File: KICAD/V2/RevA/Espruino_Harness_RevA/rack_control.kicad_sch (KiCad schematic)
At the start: 12 parts, among them Q1201 2N7002, Q1202 2N7002, U1201 MCP23017-E/SO

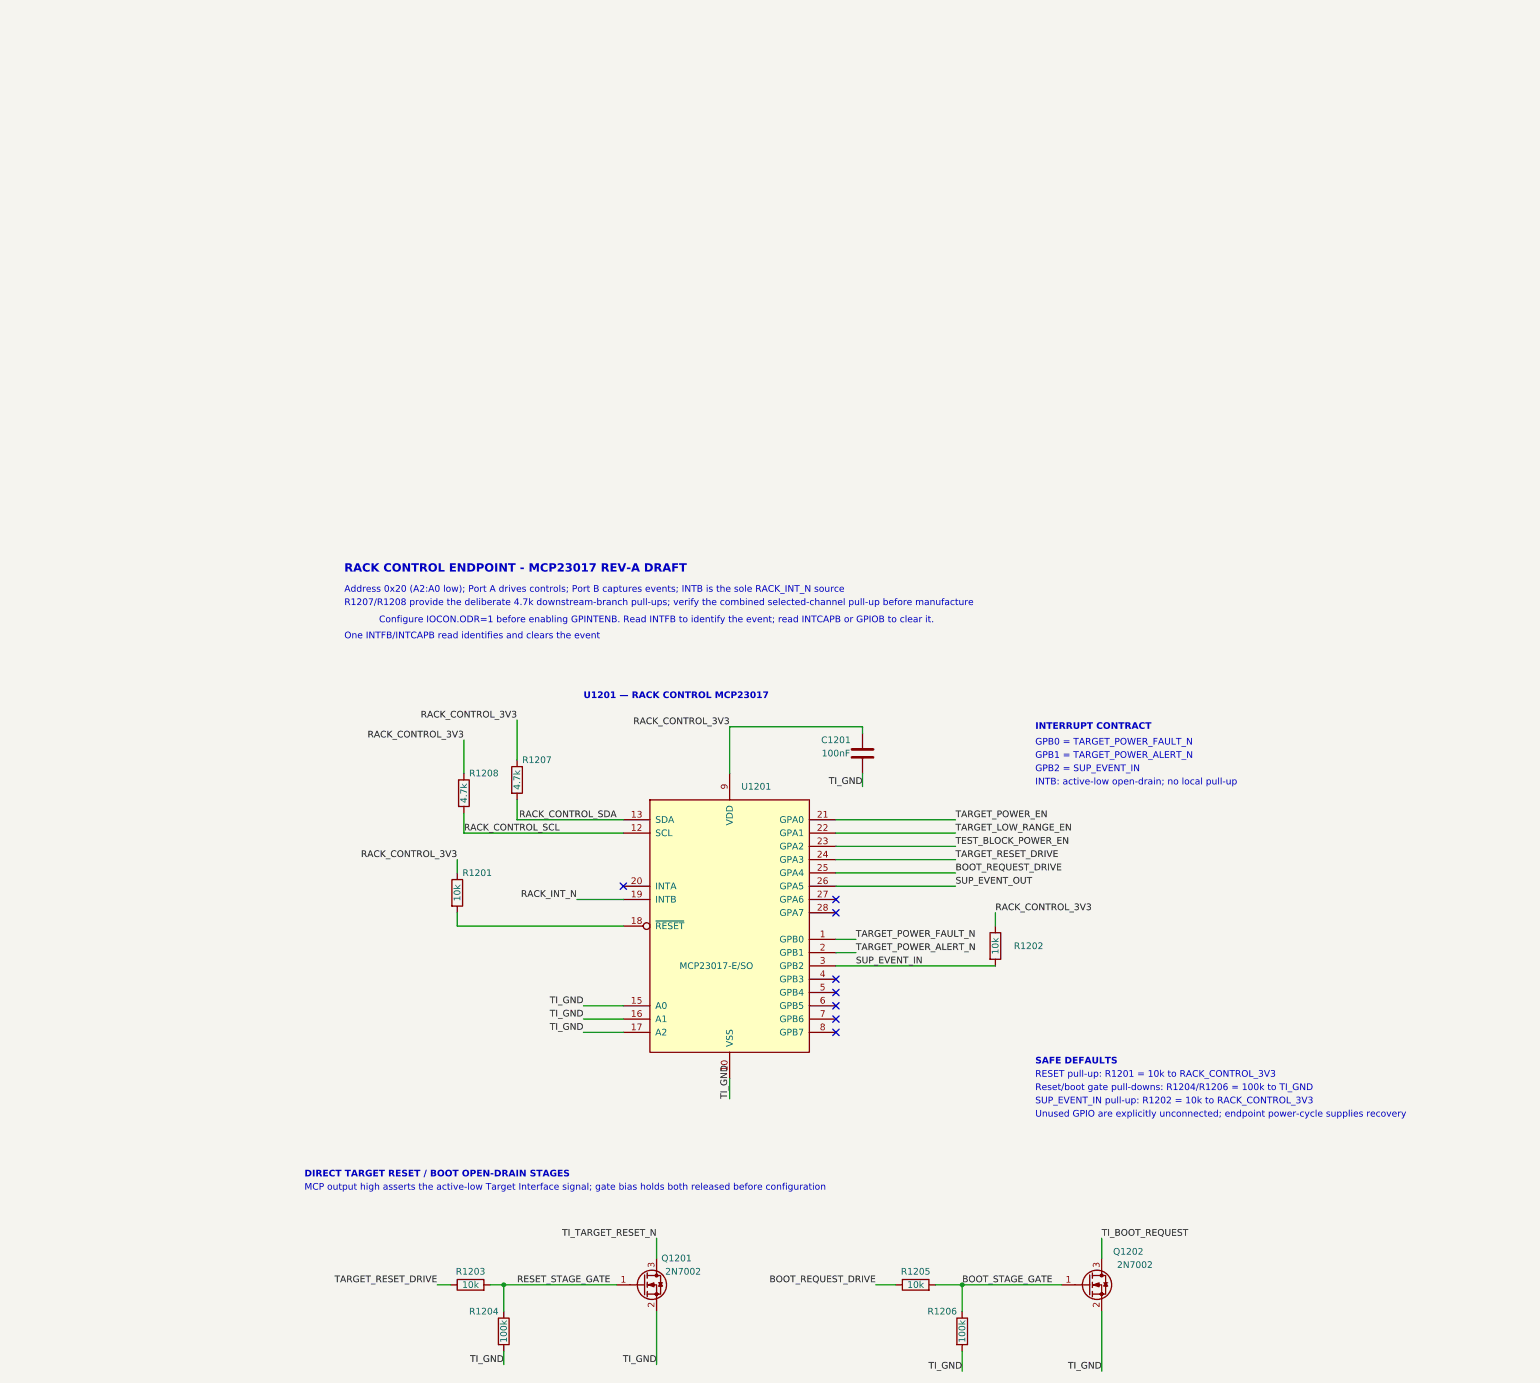
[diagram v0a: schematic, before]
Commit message: Integrate Rev-A rack control endpoint
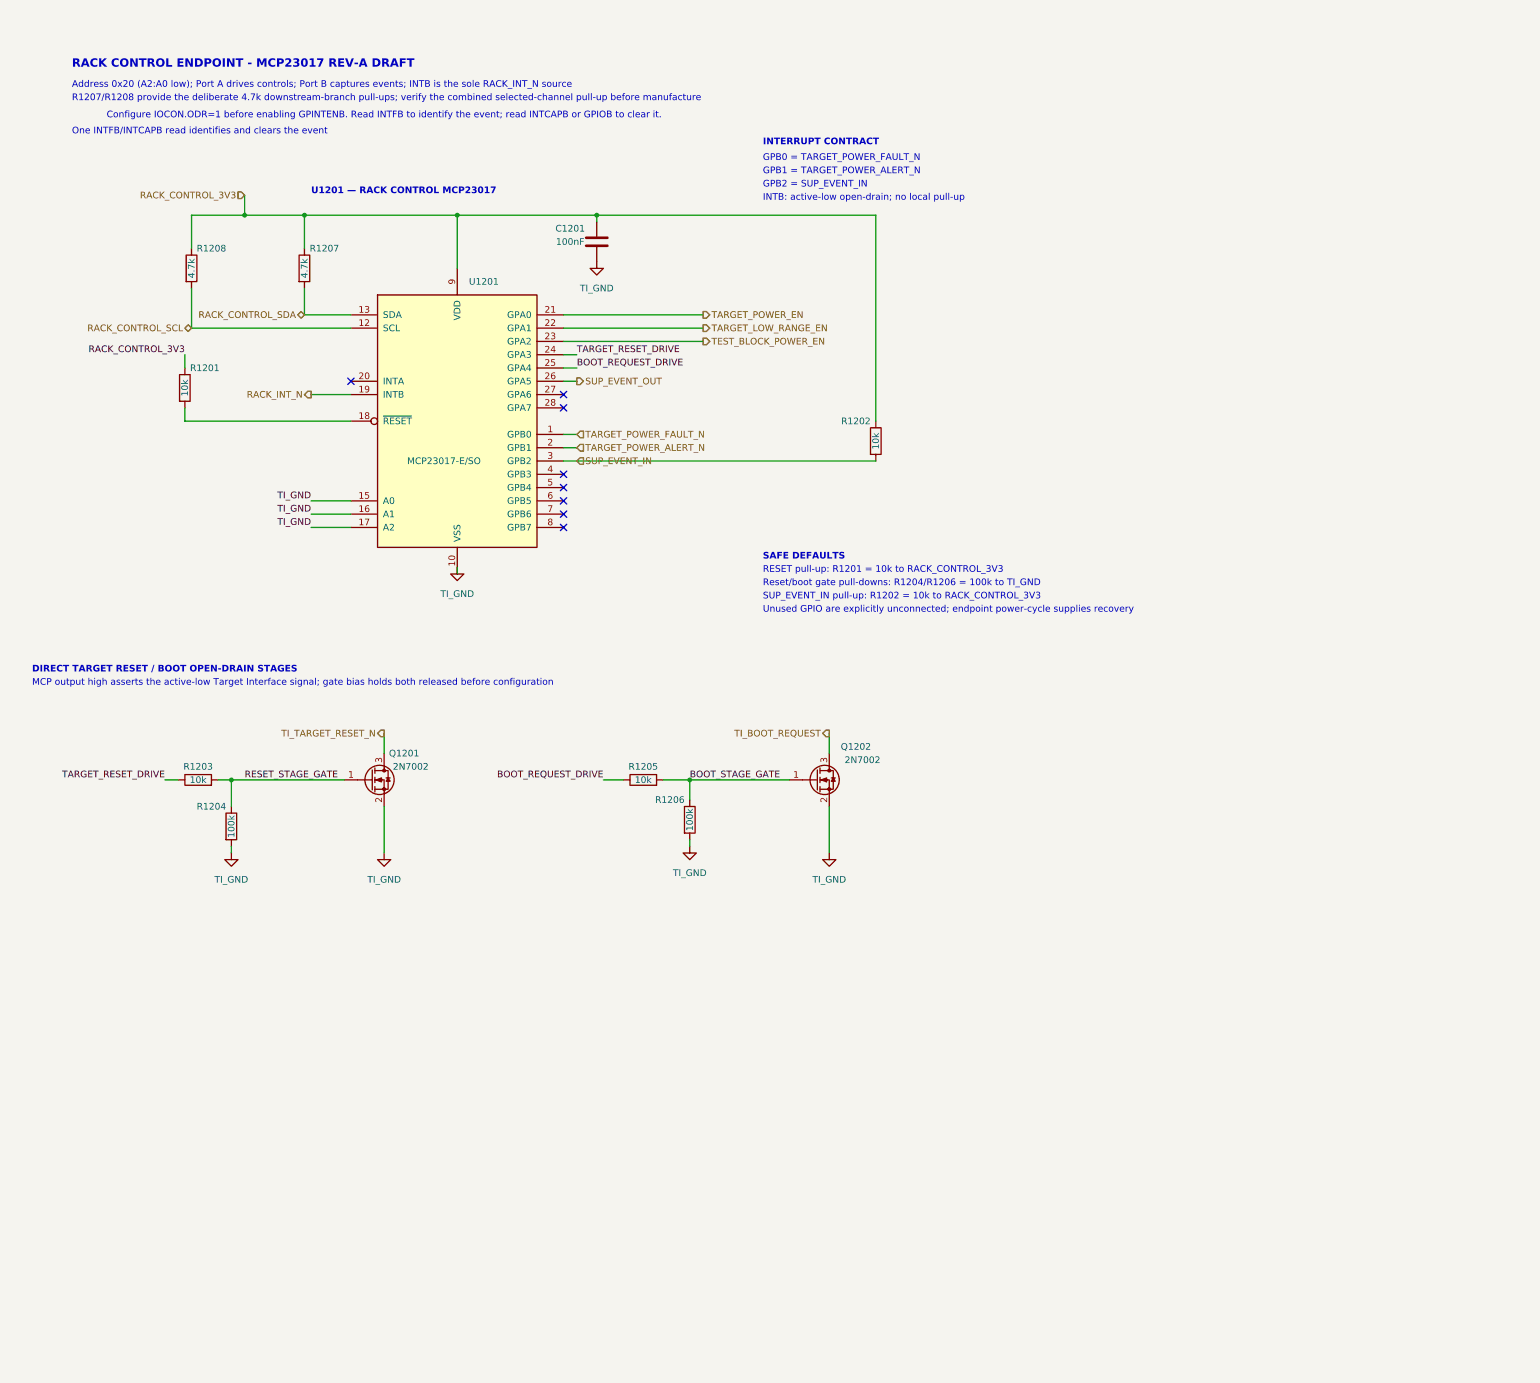
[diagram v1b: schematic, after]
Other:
- company: ESP32_SGATest -> (none)
- title: DRAFT WORKBENCH - RACK CONTROL ENDPOINT -> (none)
- moved on the sheet: C1201, Q1201, Q1202, R1201, R1202, R1203, R1204, R1205, R1206, R1207, R1208, U1201

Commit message: Implement low-range power alert integration
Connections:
- net LOW_RANGE_OK_N: now reaches U1201.4 (GPB3)
- no-connect marks 8 -> 7
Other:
- note added: "GPB3 = LOW_RANGE_OK_N"
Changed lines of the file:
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@@
 	(text "GPB1 = TARGET_POWER_ALERT_N"
 		(exclude_from_sim no)
-		(at 158.75 46.99 0)
+		(at 185.3484 98.6501 0)
 		(effects
 			(font
@@
 	(text "GPB2 = SUP_EVENT_IN"
 		(exclude_from_sim no)
-		(at 158.75 49.53 0)
+		(at 185.3484 101.1901 0)
 		(effects
 			(font
@@
 		)
 	)
+	(text "GPB3 = LOW_RANGE_OK_N"
+		(exclude_from_sim no)
+		(at 198.12 102.87 0)
+		(effects
+			(font
+				(size 1.27 1.27)
+			)
+		)
+	)
 	(text "INTB: active-low open-drain; no local pull-up"
 		(exclude_from_sim no)
-		(at 158.75 52.07 0)
+		(at 185.3484 106.2701 0)
 		(effects
 			(font
@@
 	(text "GPB0 = TARGET_POWER_FAULT_N"
 		(exclude_from_sim no)
-		(at 158.75 44.45 0)
+		(at 185.3484 96.1101 0)
 		(effects
 			(font
@@
 	(text "INTERRUPT CONTRACT"
 		(exclude_from_sim no)
-		(at 158.75 41.45 0)
+		(at 185.3484 93.1101 0)
 		(effects
 			(font
@@
 	)
 	(no_connect
-		(at 120.65 104.14)
-	)
-	(no_connect
 		(at 120.65 106.68)
 	)
@@
 		(pts
 			(xy 71.12 54.61) (xy 100.33 54.61)
+		)
+		(stroke
+			(width 0)
+			(type default)
+		)
+	)
+	(wire
+		(pts
+			(xy 120.65 104.14) (xy 123.19 104.14)
 		)
 		(stroke
@@
 		)
 	)
+	(hierarchical_label "LOW_RANGE_OK_N"
+		(shape input)
+		(at 123.19 104.14 0)
+		(effects
+			(font
+				(size 1.27 1.27)
+			)
+			(justify left)
+		)
+	)

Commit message: Implement RC01 routing baseline metadata
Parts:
- C1201: AISLER_MPN (none) -> 100nF 10% 16V X7R 0603
- R1204, R1206: AISLER_MPN (none) -> 100k 0603 1% 0.1W
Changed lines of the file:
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@@
+			)
+		)
+		(property "AISLER_MPN" "100nF 10% 16V X7R 0603"
+			(at 127 59.69 0)
+			(effects
+				(font
+					(size 1.27 1.27)
+				)
 			)
 		)
@@
 				)
 				(hide yes)
+			)
+		)
+		(property "AISLER_MPN" "100k 0603 1% 0.1W"
+			(at 57.15 171.45 0)
+			(effects
+				(font
+					(size 1.27 1.27)
+				)
 			)
 		)
@@
 			)
 		)
+		(property "AISLER_MPN" "100k 0603 1% 0.1W"
+			(at 144.78 170.18 0)
+			(effects
+				(font
+					(size 1.27 1.27)
+				)
+			)
+		)

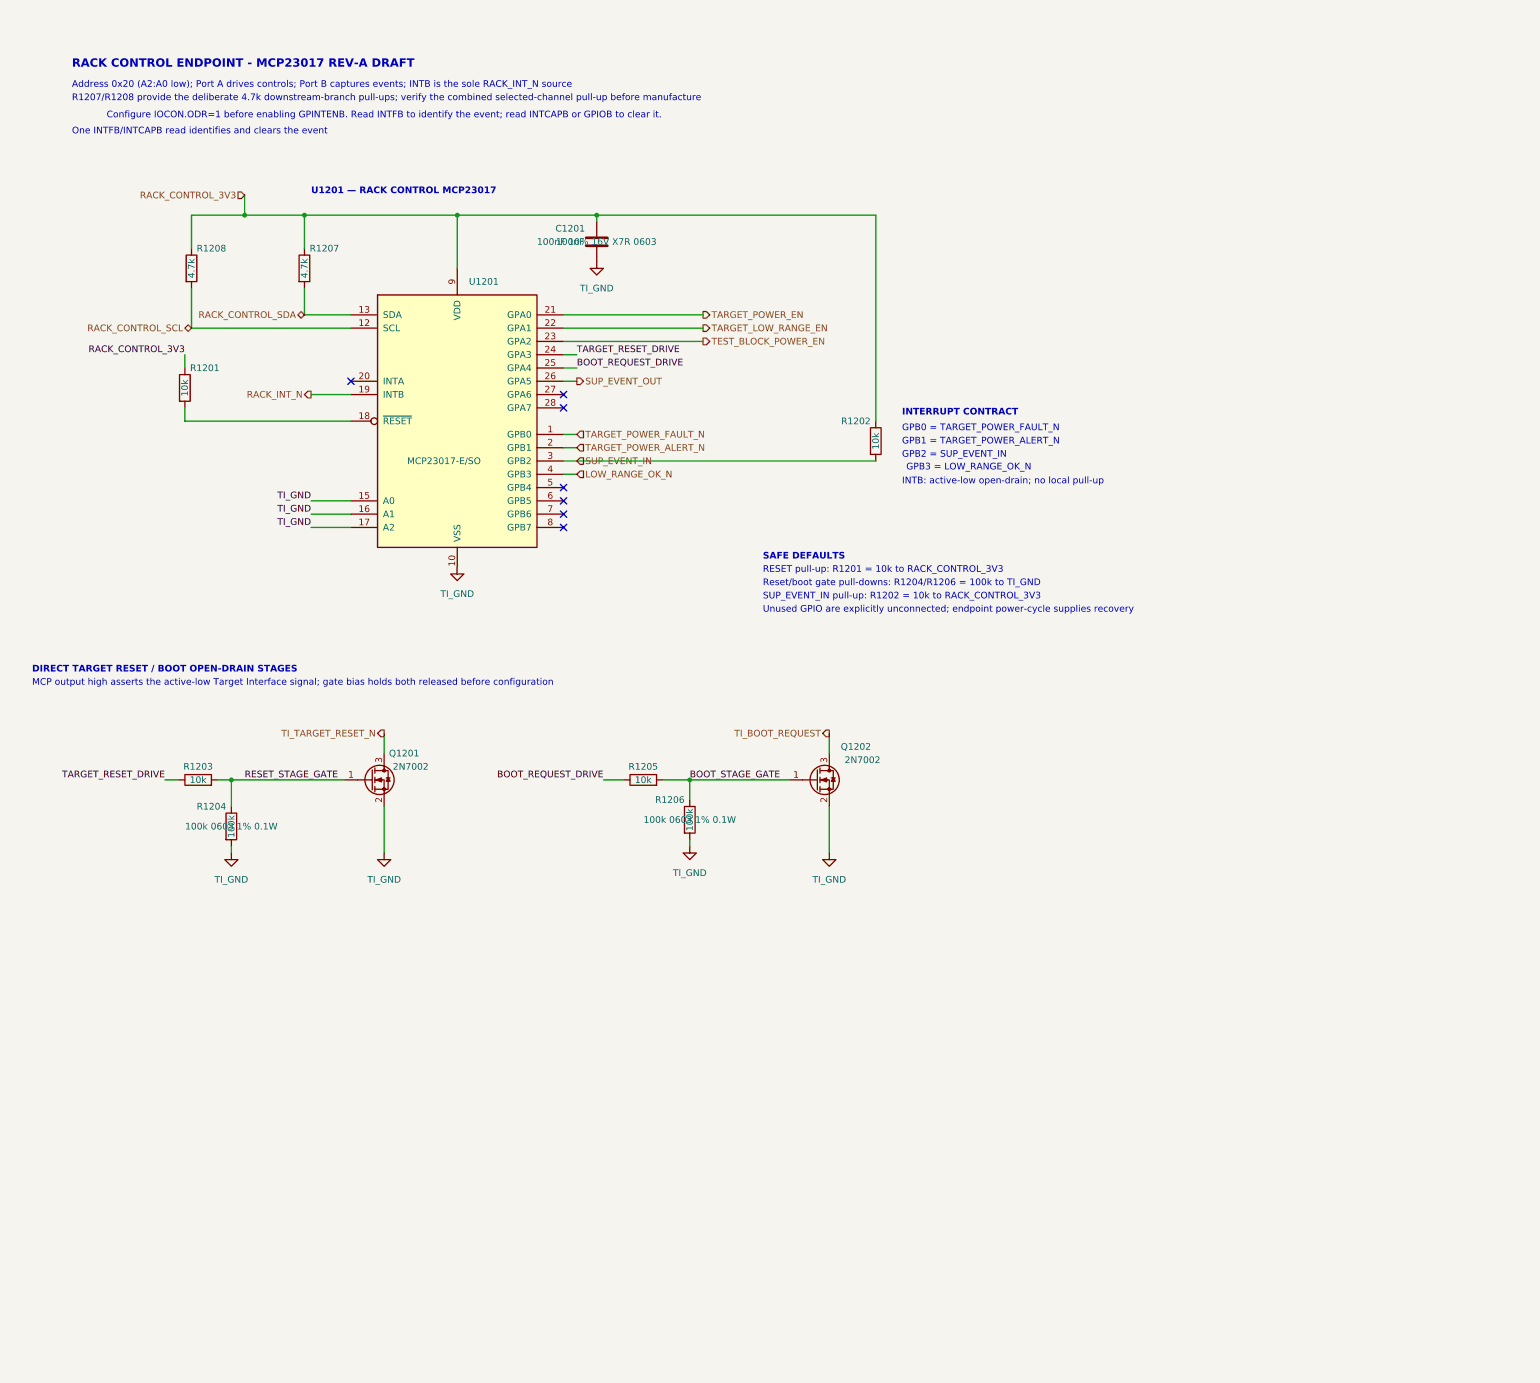
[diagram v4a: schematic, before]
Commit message: Verify RC02 routing control baseline
Add the qualified fixed-I2C isolation and Hardware Clear implementation, exact component metadata, deterministic RC02 connectivity contract, accepted ERC/connectivity evidence, and visual review records. Synchronize the draft PCB and document the PCB-stage workflow while preserving the verified RC01 baseline.
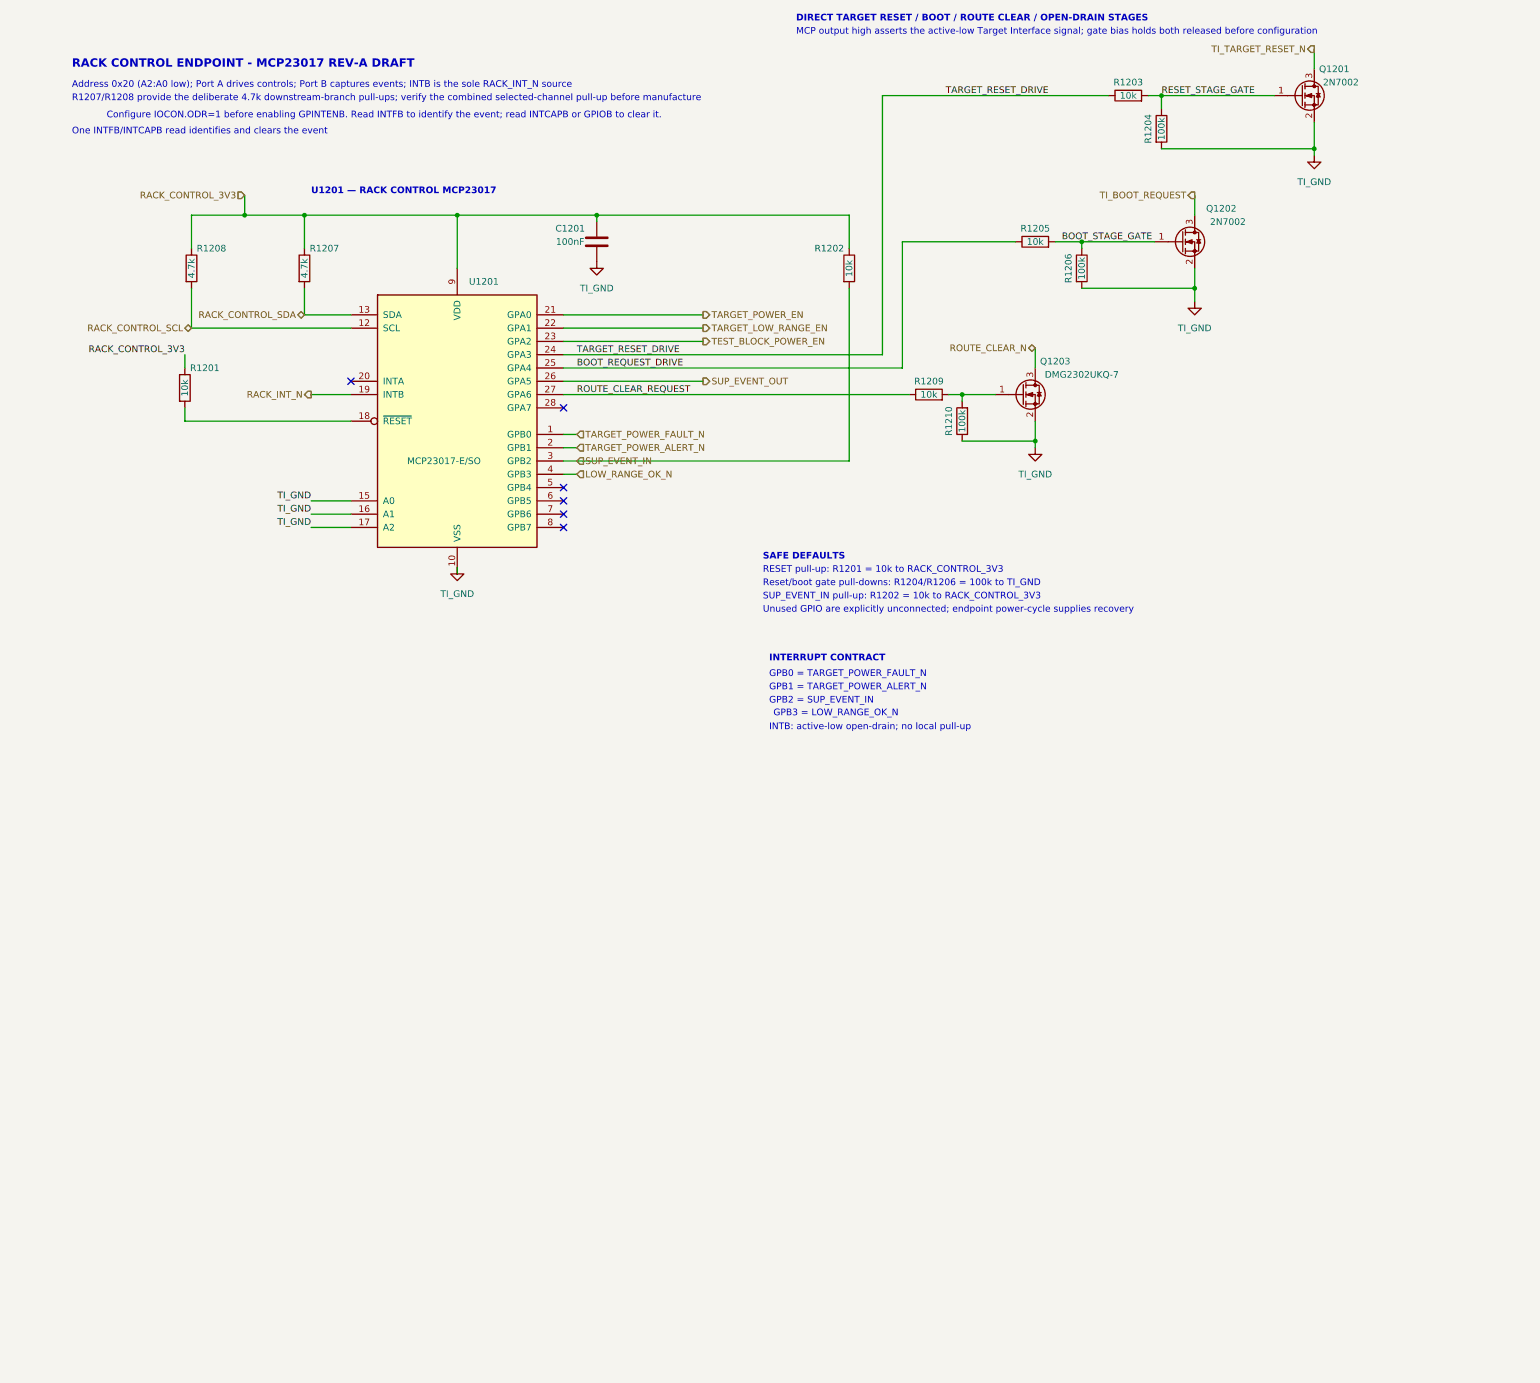
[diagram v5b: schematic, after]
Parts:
- added Q1203: DMG2302UKQ-7, Package_TO_SOT_SMD:SOT-23, symbol Espruino_Harness_RevA:NMOS_2N7002_GSD
- added R1209: 10k, Resistor_SMD:R_0603_1608Metric, symbol Espruino_Harness_RevA:R_0603
- added R1210: 100k, Resistor_SMD:R_0603_1608Metric, symbol Espruino_Harness_RevA:R_0603
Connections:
- net TI_GND: now also Q1203.2 (S), R1210.1
- net ROUTE_CLEAR_REQUEST: now reaches U1201.27 (GPA6)
- net ROUTE_CLEAR_REQUEST: now also R1209.1
- new net: Q1203.1 (G), R1209.2, R1210.2
- new net ROUTE_CLEAR_N: Q1203.3 (D)
- no-connect marks 7 -> 6
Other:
- note added: "DIRECT TARGET RESET / BOOT / ROUTE CLEAR / OPEN-DRAIN STAGES"
- note removed: "DIRECT TARGET RESET / BOOT OPEN-DRAIN STAGES"
- moved on the sheet: Q1201, Q1202, R1202, R1203, R1204, R1205, R1206
